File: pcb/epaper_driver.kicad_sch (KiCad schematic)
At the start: 1 part, among them J5 Conn_01x24_Socket

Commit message: caps
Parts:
- added C19, C20, C21, C22, C23, C24, C25, C26, C27, C28: 4.7uF, symbol Device:C_Small
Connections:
- net PREVGH: now also C24.2
- net PREVGL: now also C27.2
- net VCOM: now also C28.2
- net VDD: now also C21.2
- net VDDIO: now also C26.2
- net VGH: now also C20.1
- net VGL: now also C19.2
- net VPP: now also C22.2
- net VSH: now also C23.2
- net VSL: now also C25.2
- new net GND: C19.1, C20.2, C21.1, C22.1, C23.1, C24.1, C25.1, C26.1, C27.1, C28.1

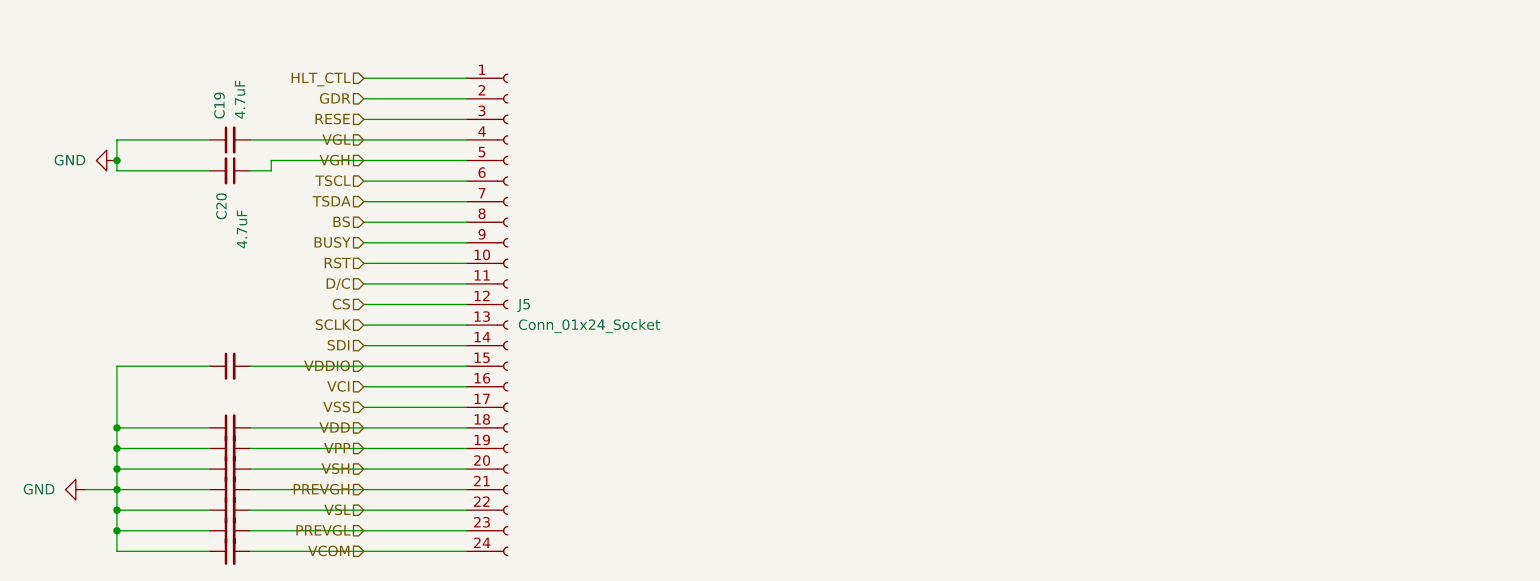
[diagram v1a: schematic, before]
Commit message: pcb: Schematics seem complete
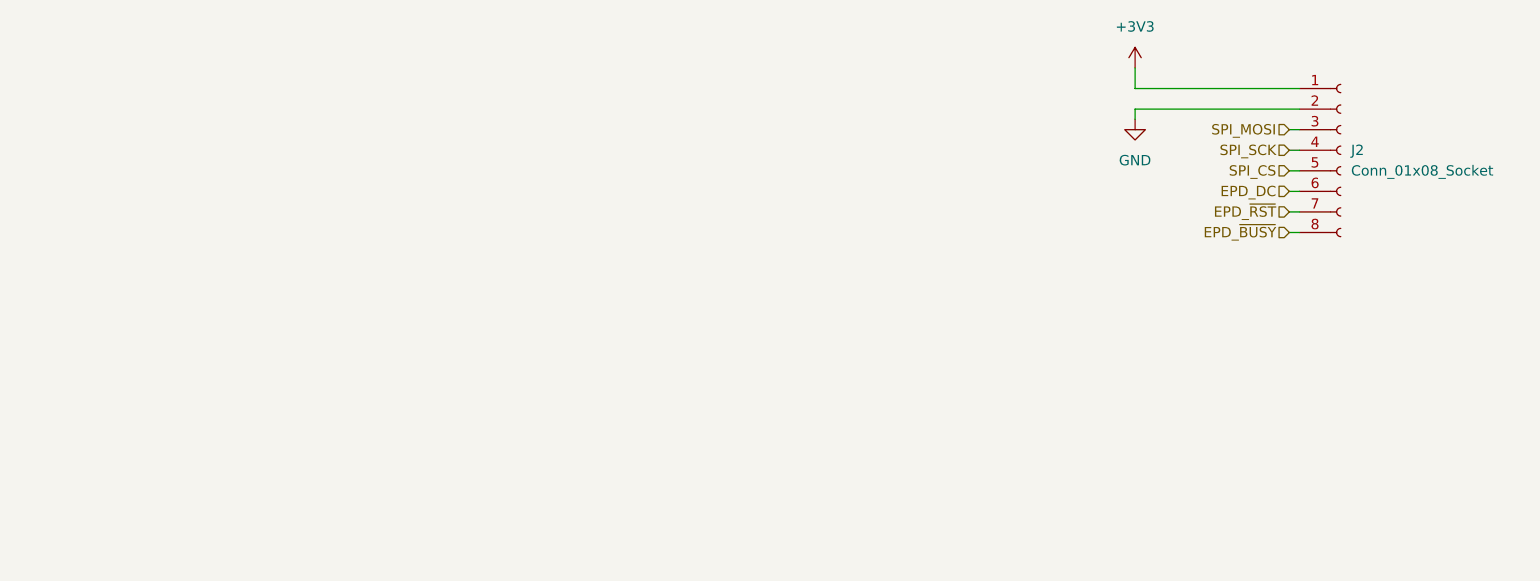
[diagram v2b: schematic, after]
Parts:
- removed C19, C20, C21, C22, C23, C24, C25, C26, C27, C28: 4.7uF, symbol Device:C_Small
- removed J5: Conn_01x24_Socket, symbol Connector:Conn_01x24_Socket
- added J2: Conn_01x08_Socket, symbol Connector:Conn_01x08_Socket
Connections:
- net GND: now also J2.2 (Pin_2)
- new net +3V3: J2.1 (Pin_1)
- new net EPD_DC: J2.6 (Pin_6)
- new net EPD_~{BUSY}: J2.8 (Pin_8)
- new net EPD_~{RST}: J2.7 (Pin_7)
- new net SPI_CS: J2.5 (Pin_5)
- new net SPI_MOSI: J2.3 (Pin_3)
- new net SPI_SCK: J2.4 (Pin_4)
